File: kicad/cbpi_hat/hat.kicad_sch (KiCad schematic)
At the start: 30 parts, among them J1 GPIO, J2 Screw_Terminal_01x02, Q1 HY15P03C2, U1 CAT24C256, U2 EUP3453WIR1

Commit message: Added protection against back powering. This should fix #12
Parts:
- added Q2: DMG2305UX, dmg2305ux:SOT-23-3_L2.9-W1.3-P0.95-LS2.4-BR-1, symbol dmg2305ux:DMG2305UX
- added Q3: DMMT5401-7-F, dmmt5401-f-7:SOT-23-6_L2.9-W1.6-P0.95-LS2.8-BR, symbol dmmt5401-f-7:DMMT5401-7-F
- added R10: 10k, Resistor_SMD:R_0402_1005Metric, symbol Device:R
- added R11: 47k, Resistor_SMD:R_0402_1005Metric, symbol Device:R
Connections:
- net +5V: now also Q2.3 (D), Q3.6 (E1); no longer J1.2 (Pin_2), J1.4 (Pin_4)
- net GND: now also R10.2, R11.2
- new net: Q3.1 (C1), Q3.2 (B1), Q3.3 (B2), R10.1
- new net: Q2.1 (G), Q3.4 (C2), R11.1
- new net +5VD: J1.2 (Pin_2), J1.4 (Pin_4), Q2.2 (S), Q3.5 (E2)

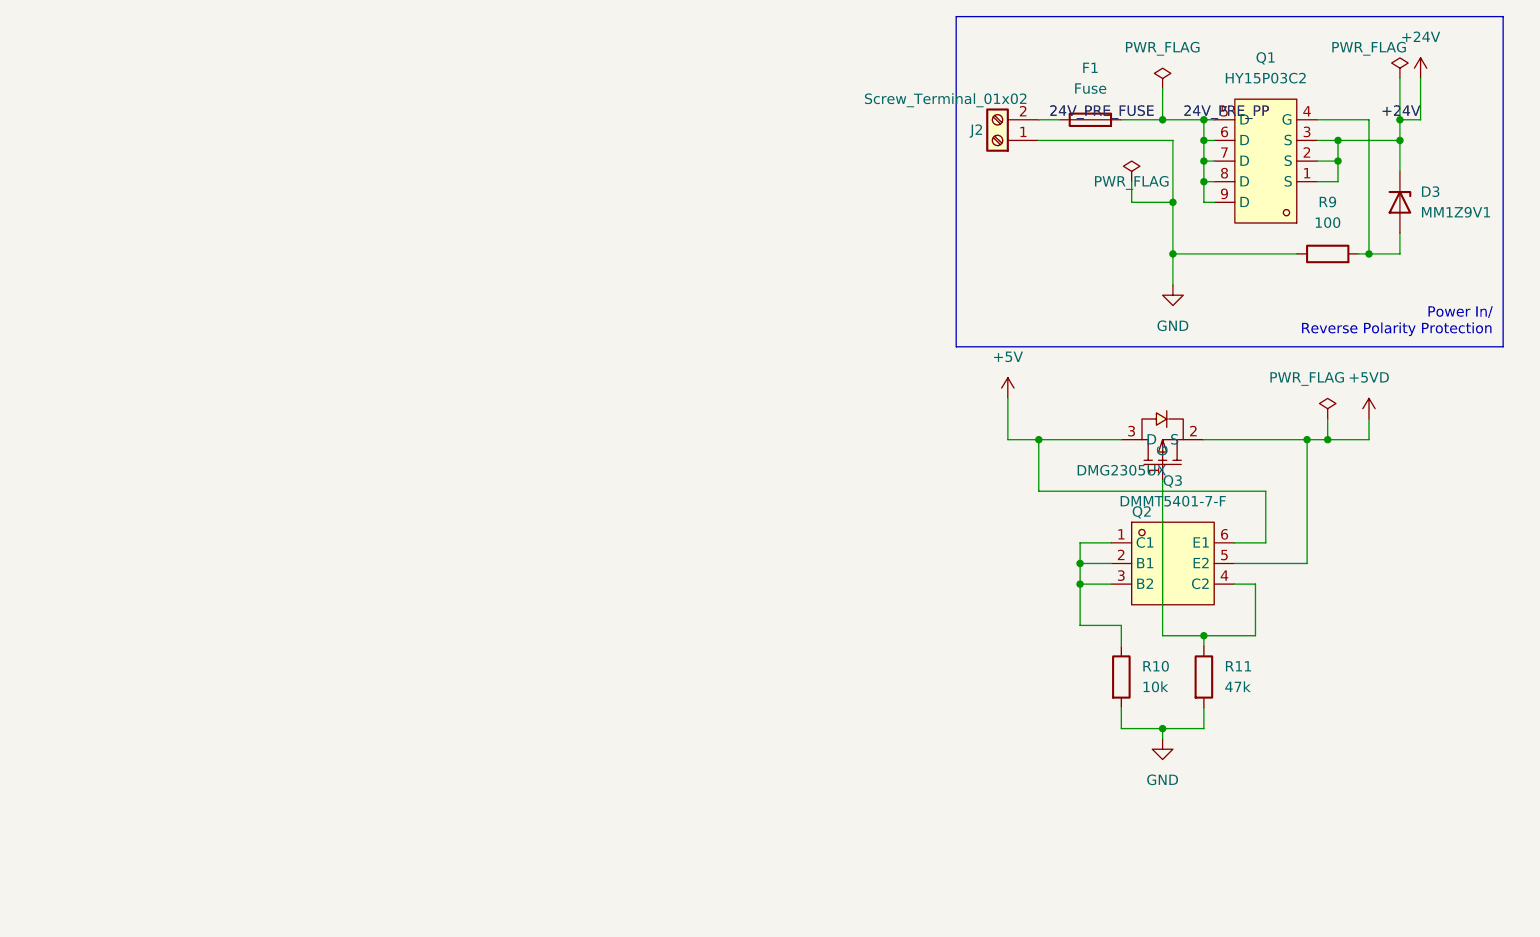
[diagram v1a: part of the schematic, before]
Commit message: DC-DC converter and identity eeprom should be fully routed now (except for GND).
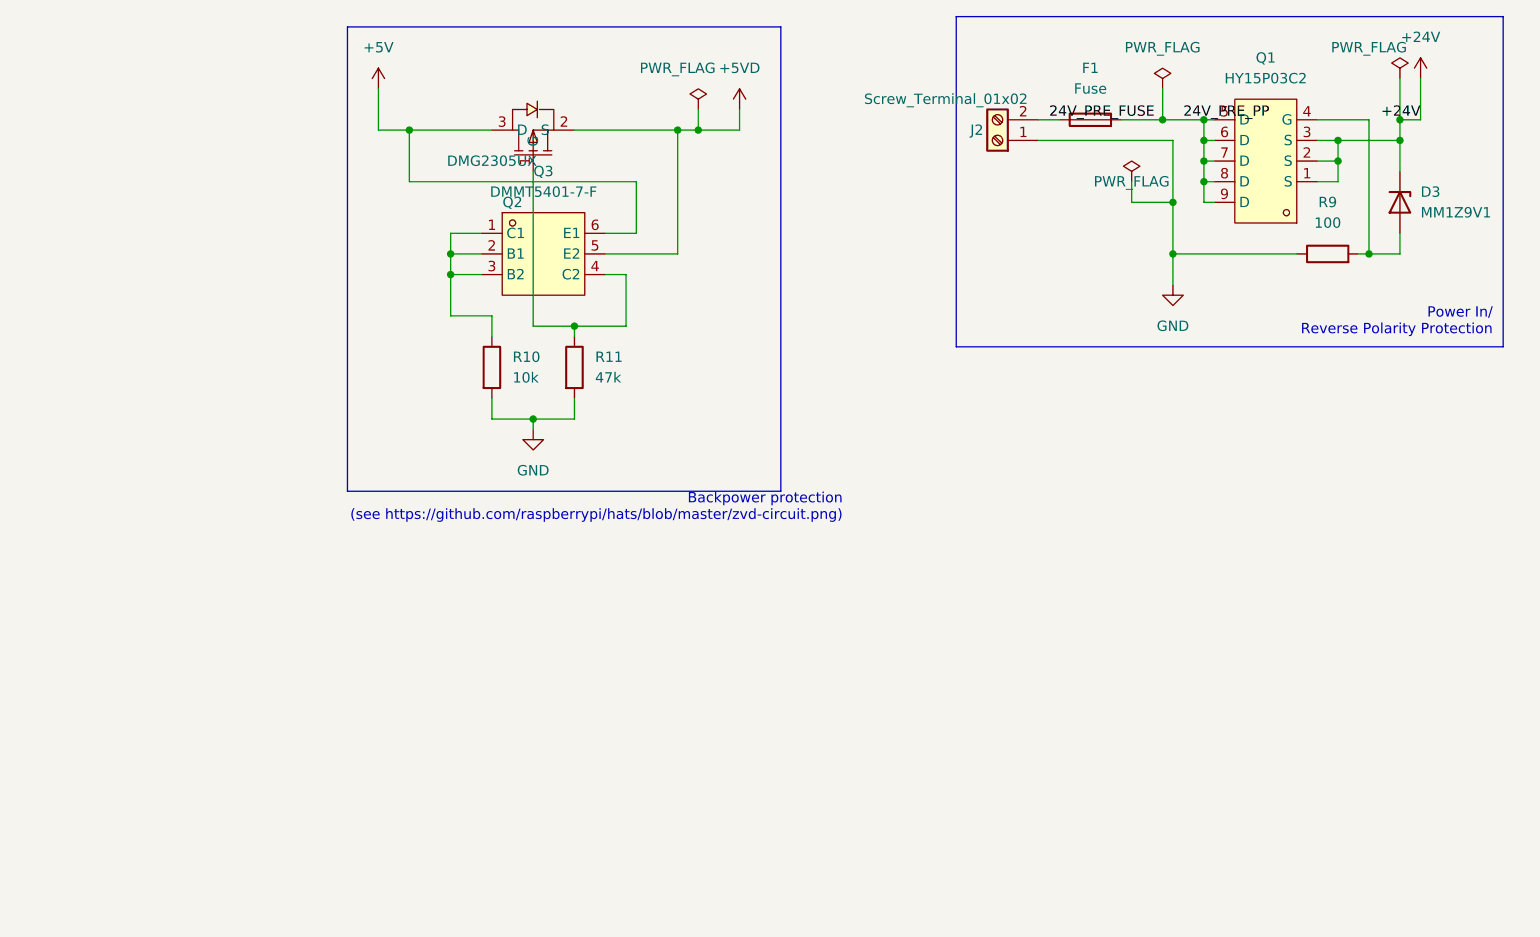
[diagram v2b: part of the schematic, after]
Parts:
- R9: footprint Resistor_SMD:R_01005_0402Metric -> Resistor_SMD:R_0402_1005Metric
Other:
- note added: "Backpower protection (see https://github.com/raspberrypi/hats/blob/master/zvd-circuit.png)"
- moved on the sheet: Q2, Q3, R10, R11

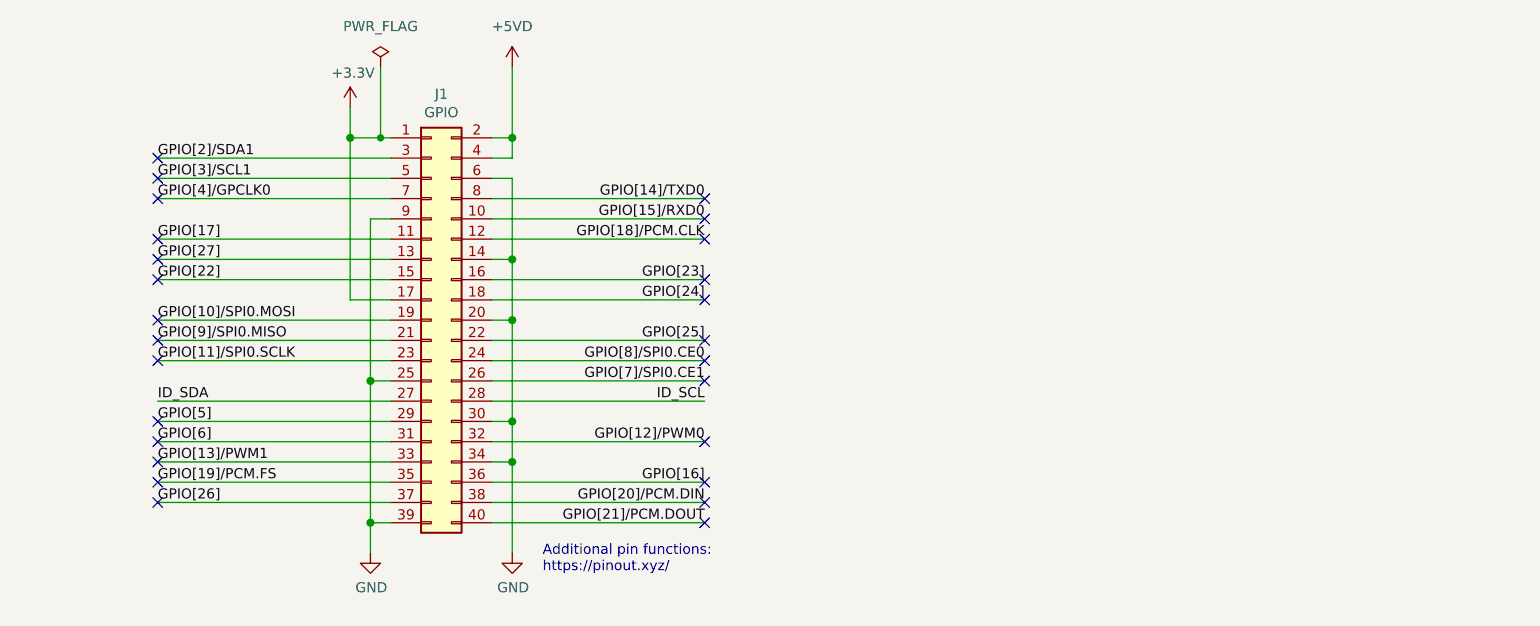
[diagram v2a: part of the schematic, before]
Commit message: RTC is now in the schematic
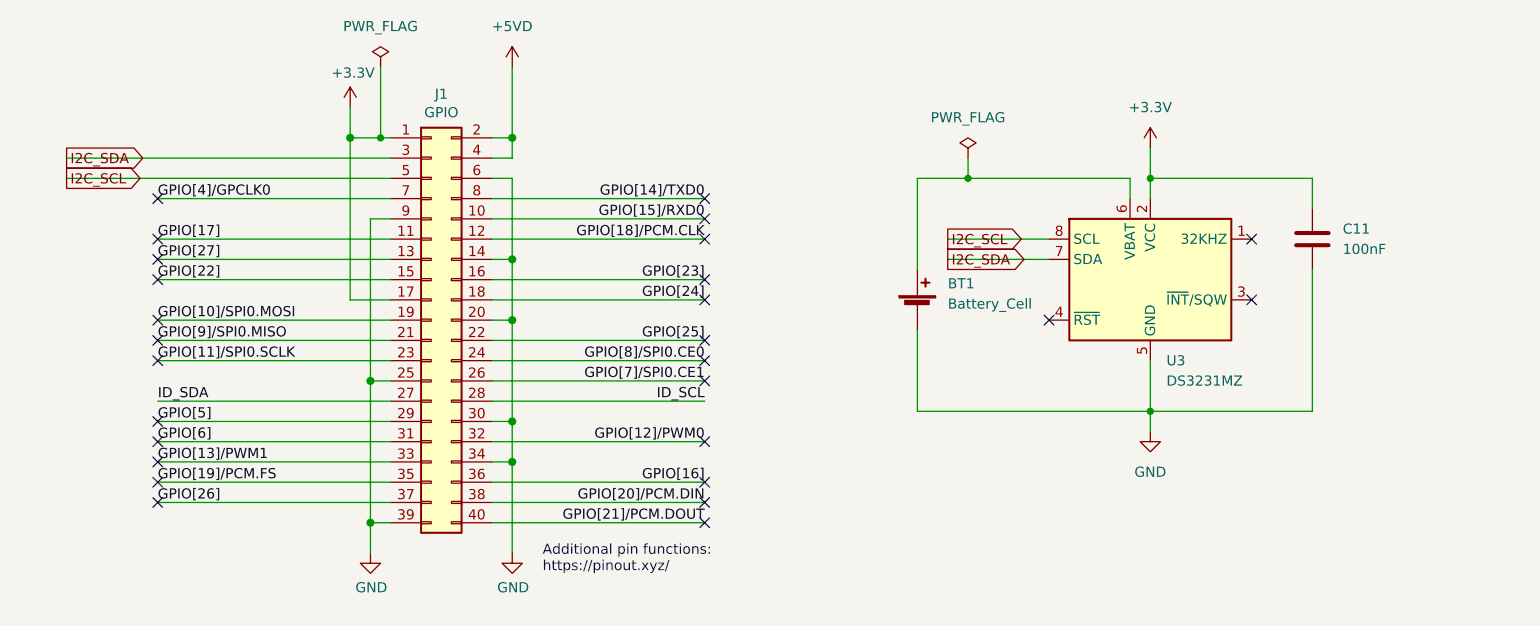
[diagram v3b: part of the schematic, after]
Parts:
- added BT1: Battery_Cell, symbol Device:Battery_Cell
- added C11: 100nF, symbol Device:C
- added U3: DS3231MZ, Package_SO:SOIC-8_3.9x4.9mm_P1.27mm, symbol Timer_RTC:DS3231MZ
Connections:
- net +3.3V: now also C11.1, U3.2 (VCC)
- net GND: now also BT1.2 (-), C11.2, U3.5 (GND)
- net GPIO[2]/SDA1 renamed I2C_SDA
- net I2C_SDA: now also U3.7 (SDA)
- net GPIO[3]/SCL1 renamed I2C_SCL
- net I2C_SCL: now also U3.8 (SCL)
- new net: BT1.1 (+), U3.6 (VBAT)
- no-connect marks 30 -> 31

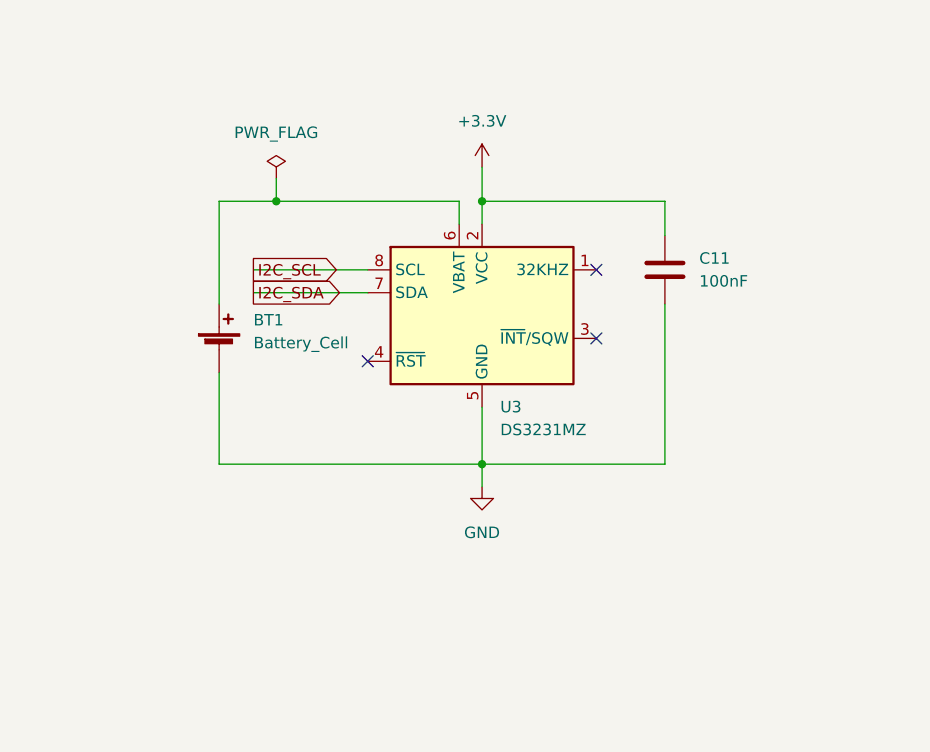
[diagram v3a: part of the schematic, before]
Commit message: RTC block is now annotated
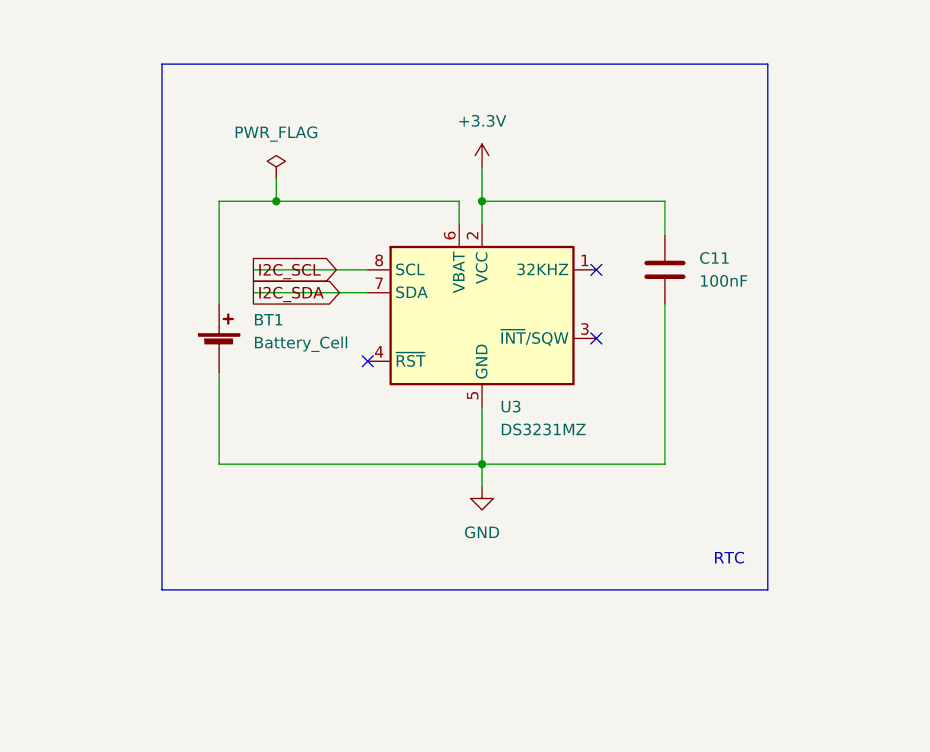
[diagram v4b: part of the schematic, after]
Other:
- note added: "RTC"
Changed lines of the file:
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@@
     (stroke (width 0) (type solid) (color 0 0 0 0))
+  )
+  (polyline (pts (xy 187.96 76.2) (xy 120.65 76.2))
+    (stroke (width 0) (type default) (color 0 0 0 0))
   )
   (wire (pts (xy 516.89 53.34) (xy 525.78 53.34))
@@
     (stroke (width 0) (type default) (color 0 0 0 0))
   )
+  (polyline (pts (xy 187.96 17.78) (xy 187.96 76.2))
+    (stroke (width 0) (type default) (color 0 0 0 0))
+  )
   (wire (pts (xy 93.98 172.72) (xy 93.98 175.26))
     (stroke (width 0) (type solid) (color 0 0 0 0))
@@
     (stroke (width 0) (type default) (color 0 0 0 0))
   )
+  (polyline (pts (xy 120.65 17.78) (xy 120.65 76.2))
+    (stroke (width 0) (type default) (color 0 0 0 0))
+  )
   (wire (pts (xy 342.9 25.4) (xy 342.9 41.91))
     (stroke (width 0) (type default) (color 0 0 0 0))
@@
   )
   (wire (pts (xy 220.98 26.67) (xy 224.79 26.67))
+    (stroke (width 0) (type default) (color 0 0 0 0))
+  )
+  (polyline (pts (xy 120.65 17.78) (xy 187.96 17.78))
     (stroke (width 0) (type default) (color 0 0 0 0))
   )
@@
     (effects (font (size 1.27 1.27)) (justify left bottom))
   )
+  (text "RTC" (at 185.42 73.66 180)
+    (effects (font (size 1.27 1.27)) (justify right bottom))
+  )
   (text "Backpower protection\n(see https://github.com/raspberrypi/hats/blob/master/zvd-circuit.png)"

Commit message: Added RTC to board
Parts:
- BT1: footprint (none) -> cr2032-bs-6-1:BAT-TH_CR2032-BS-6-1
- C11: footprint (none) -> Capacitor_SMD:C_0603_1608Metric
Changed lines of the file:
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@@
       (effects (font (size 1.27 1.27)) (justify left))
     )
-    (property "Footprint" "" (id 2) (at 127 48.006 90)
+    (property "Footprint" "cr2032-bs-6-1:BAT-TH_CR2032-BS-6-1" (id 2) (at 127 48.006 90)
       (effects (font (size 1.27 1.27)) hide)
     )
@@
       (effects (font (size 1.27 1.27)) (justify left))
     )
-    (property "Footprint" "" (id 2) (at 177.4952 44.45 0)
+    (property "Footprint" "Capacitor_SMD:C_0603_1608Metric" (id 2) (at 177.4952 44.45 0)
       (effects (font (size 1.27 1.27)) hide)
     )
@@
     )
     (path "/4c443932-87d8-4252-a612-8cadafc00eb7"
-      (reference "BT1") (unit 1) (value "Battery_Cell") (footprint "")
+      (reference "BT1") (unit 1) (value "Battery_Cell") (footprint "cr2032-bs-6-1:BAT-TH_CR2032-BS-6-1")
     )
     (path "/0f7872a7-de47-41d5-a21f-9934102d3a5f"
@@
     )
     (path "/a85f2efb-cd8d-410a-8aad-af69ccb88a31"
-      (reference "C11") (unit 1) (value "100nF") (footprint "")
+      (reference "C11") (unit 1) (value "100nF") (footprint "Capacitor_SMD:C_0603_1608Metric")
     )
     (path "/95466bc2-2f9a-4e01-98ff-50b74edc683e"
